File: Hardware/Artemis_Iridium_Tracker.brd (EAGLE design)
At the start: 50.8 x 63.5 mm, 197 parts, among them J1 IRIDIUM_9603N, J2 USB-C, J6 uFL, J7 ANTENNA-GROUNDEDEDGE_SMA, Q1 DMG3414U-7, Q2 DMG3415U-7, Q3 DMG3415U-7, Q4 2N2222, U1 CH340E_MSOP10, U10 MCP111T-240E/TT, U11 3.3V, U2 LTC3225EDDB#TRMPBF, U3 ADM4210-1, U4 UBLOX_ZOE_M8-0-10, U5 AS179-92LF, U6 MS8607-02BA01, U7 ARTEMIS_MODULESMD, U9 MCP73831, X1 32.768kHz, X2 32.768kHz

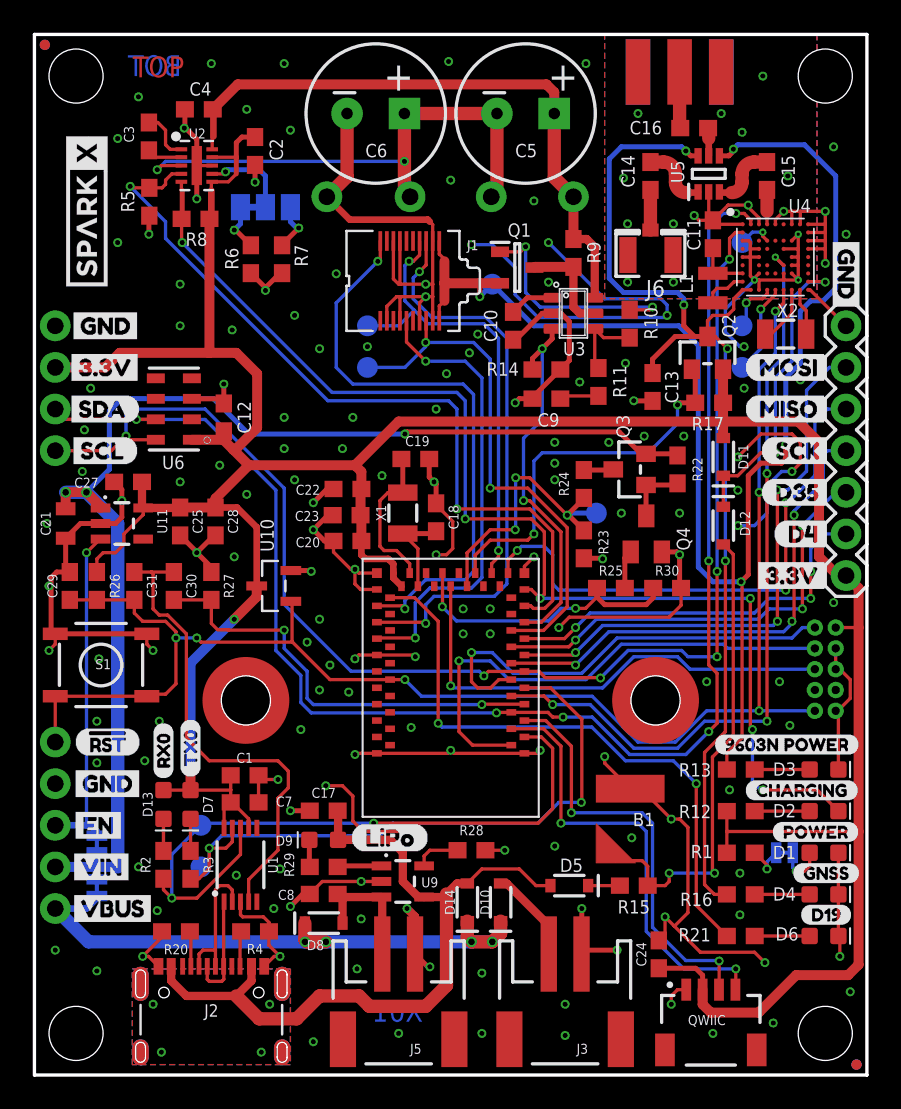
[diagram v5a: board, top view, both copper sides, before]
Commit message: Updated the PCB - tidied up the libraries
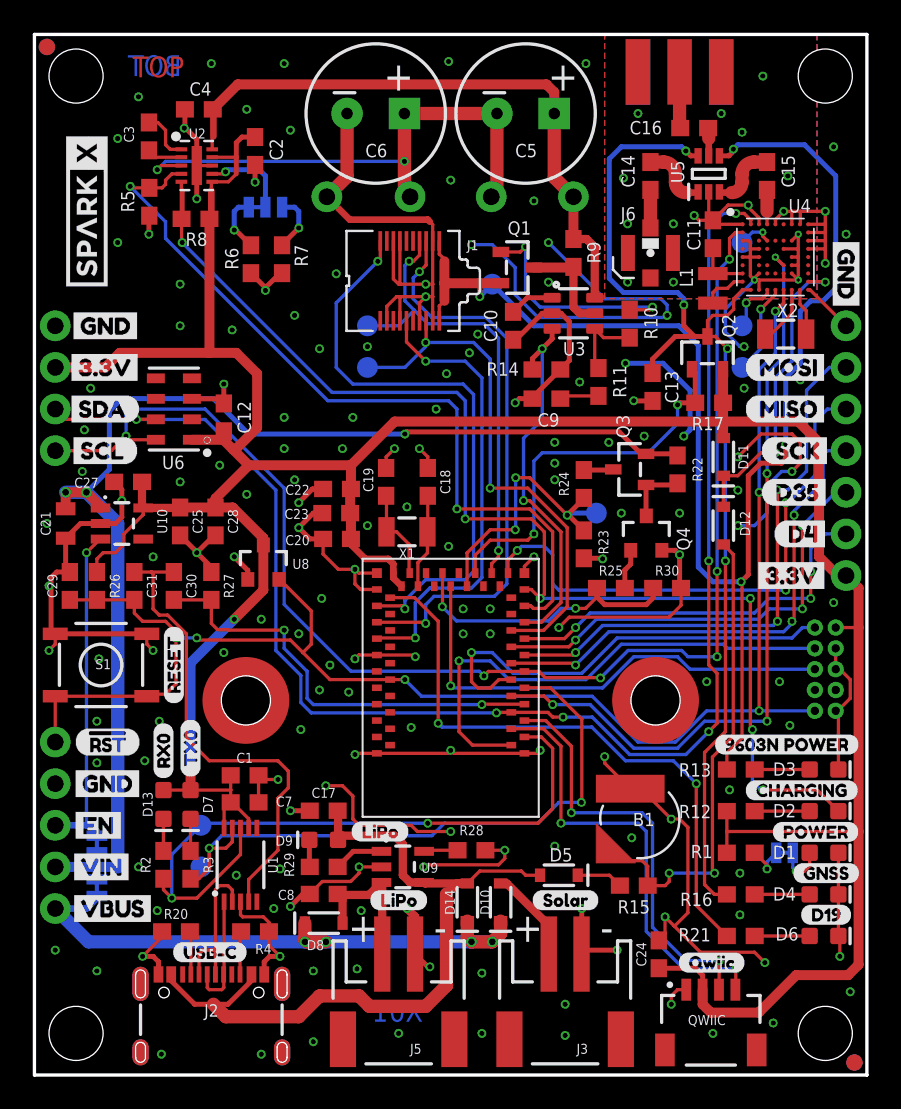
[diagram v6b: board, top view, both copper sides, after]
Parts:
- removed U11: 3.3V, SparkFun-IC-Power:SOT23-5
- added SPARKX1, SPARKX2: SPARKX-LOGO4, SparkX:SPARKX-MEDIUM
- added U$45, U$46: (no value), LiPo_0.03:LIPO0
- added U$53: (no value), USB-C:USB#C0
- added U$56: (no value), USB-C_0.03:USB#C0
- added U8: V_SUPERVISORBD48K24G-TL, New_Parts:SSOP3
- 3V3EN, MEAS: value (none) -> JUMPER-SMT_2_NC_TRACE_SILK
- I2C: device SparkX:1X04_NO_SILK -> SparkFun-Connectors:1X04_NO_SILK
- J1: device Qwiic_Iridium_9603N:IRIDIUM_9603N -> New_Parts:IRIDIUM_9603N
- J6: value uFL -> U.FL; device microbuilder:U.FL -> SparkFun-Connectors:U.FL
- J7: device Qwiic_Iridium_9603N:SMA-EDGE -> SparkFun-RF:SMA-EDGE
- JP1: value JUMPER-PAD-3-2OF3_NC_BY_TRACE_LARGE -> JUMPER-SMT_3_1-NC_TRACE_SILK; device Qwiic_Iridium_9603N:PAD-JUMPER-3-2OF3_NC_BY_TRACE_YES_SILK_LARGE -> SparkFun-Jumpers:SMT-JUMPER_3_1-NC_TRACE_SILK
- JP10, JP11, JP12, JP9: device SparkFun:STAND-OFF -> SparkFun-Hardware:STAND-OFF
- JP13, JP14, JP7, JP8: value FIDUCIALUFIDUCIAL -> FIDUCIAL1X2; device SparkFun:MICRO-FIDUCIAL -> SparkFun-Aesthetics:FIDUCIAL-1X2
- Q1: device DMG3414U-7:SOT96P240X100-3N -> New_Parts:SOT23-R
- Q2, Q3: device microbuilder:SOT23-WIDE -> New_Parts:SOT23-R
- Q4: value 2N2222 -> 600mA/40V; device transistor:SOT23-BEC -> SparkFun-DiscreteSemi:SOT23-3
- QWIIC: value (none) -> QWIIC_RIGHT_ANGLE
- R13, R5: device SparkFun-Resistors:0603@1 -> SparkFun-Resistors:0603
- R26, R27: device SparkFun-Resistors:0603@2 -> SparkFun-Resistors:0603
- R9: value 0.012 Ohm -> 0.012R; device SparkFun-Resistors:0603 -> New_Parts:0603
- SPI: device SparkFun-Connectors:1X07 -> SparkFun-Connectors:1X07_NO_SILK
- U$29: value SPARKX-LOGO4 -> (none); device SparkX:SPARKX-MEDIUM -> Solar_0.03:SOLAR0
- U$30: value SPARKX-LOGO4 -> (none); device SparkX:SPARKX-MEDIUM -> Qwiic_0.03:QWIIC0
- U$33: device RX:RX0 -> Rx:RX0
- U$37: device TX:TX0 -> Tx:TX0
- U$49: device LiPo:LIPO0 -> RESET_0.03:RESET0
- U10: value MCP111T-240E/TT -> 3.3V; device Microchip-MCP11:SOT95P237X112-3N -> SparkFun-IC-Power:SOT23-5
- U2: device Qwiic_Iridium_9603N:DFN300X200-10L -> New_Parts:DFN300X200-10L
- U3: device ADM4210:TSOT6 -> New_Parts:TSOT6
- U5: device SamacSys_Parts:SOT65P220X100-6N -> New_Parts:SOT65P220X100-6N
- U6: device SamacSys_Parts:MS8607-02BA01 -> New_Parts:MS8607-02BA01
- moved U$30 58.3 mm to (39.2, 6.86), turned to 0 degrees
- moved U$49 13.5 mm to (8.51, 22.6), turned to 90 degrees
- moved U10 10.0 mm to (5.33, 33.7), turned to 270 degrees
- moved U$29 8.56 mm to (30.4, 10.7), flipped to the top
- moved C19 2.26 mm to (21.5, 36.2), turned to 270 degrees
- moved C18 2.22 mm to (24.0, 36.2)
- moved X1 1.17 mm to (22.7, 33.1), turned to 0 degrees
- moved D5 0.90 mm to (32.0, 12.2)
- moved U9 0.89 mm to (22.5, 12.7)
- moved C23 0.65 mm to (18.4, 34.3)
- moved C20 0.65 mm to (18.5, 32.7)
- moved C22 0.63 mm to (18.5, 35.8)
- moved L1 0.38 mm to (41.4, 48.0)
- moved JP13 0.18 mm to (50.0, 0.76)
- moved JP14 0.18 mm to (0.76, 62.7)
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- renumbered RX(OUT) to RX1, TX(IN) to TX1
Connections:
- removed net SHLD: J2.SHLD1, J2.SHLD2, J2.SHLD3, J2.SHLD4, J2.SHLD5, J2.SHLD6, J2.SHLD7, J2.SHLD8
- net 3.3V: now also U10.5, U8.3; no longer U10.3, U11.5
- net ARTEMIS_!RESET: now also U8.2; no longer U10.1
- net GND: now also Q4.2, U8.1; no longer Q4.E, U11.2
- net IRIDIUM: now also J6.FEED; no longer J6.3
- net N$36: now also U10.3; no longer U11.3
- net N$37: now also Q4.3; no longer Q4.C
- net N$47: now also Q4.1; no longer Q4.B
- net VIN: now also U10.1; no longer U11.1
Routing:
- net GND: track 293.3 -> 307.7 mm, vias 169 -> 177
- net N$31: track 9.31 -> 5.67 mm
- net ARTEMIS_!RESET: track 92.6 -> 95.6 mm
- net V_BATT: track 8.15 -> 9.31 mm
- net D-2: track 8.48 -> 9.46 mm
- net N$20: track 1.94 -> 2.84 mm
- net N$39: track 2.79 -> 2.07 mm
- net V_USB: track 46.2 -> 46.8 mm
- net N$4: track 3.03 -> 3.61 mm
- net N$2: track 2.96 -> 3.54 mm
- net D+2: track 6.66 -> 7.18 mm
- removed copper zone on layer 1, net SHLD
- removed copper zone on layer 16, net SHLD

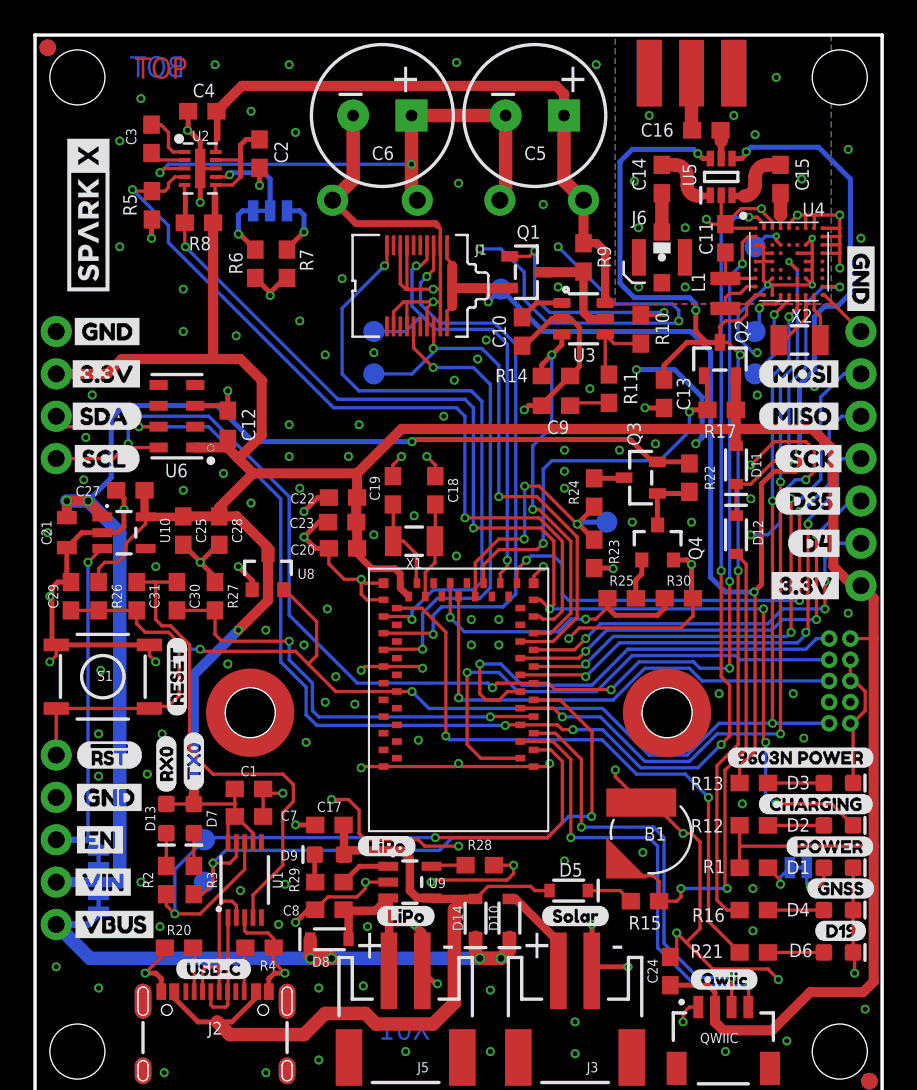
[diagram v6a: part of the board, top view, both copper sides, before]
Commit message: Updated the PCB and the examples README
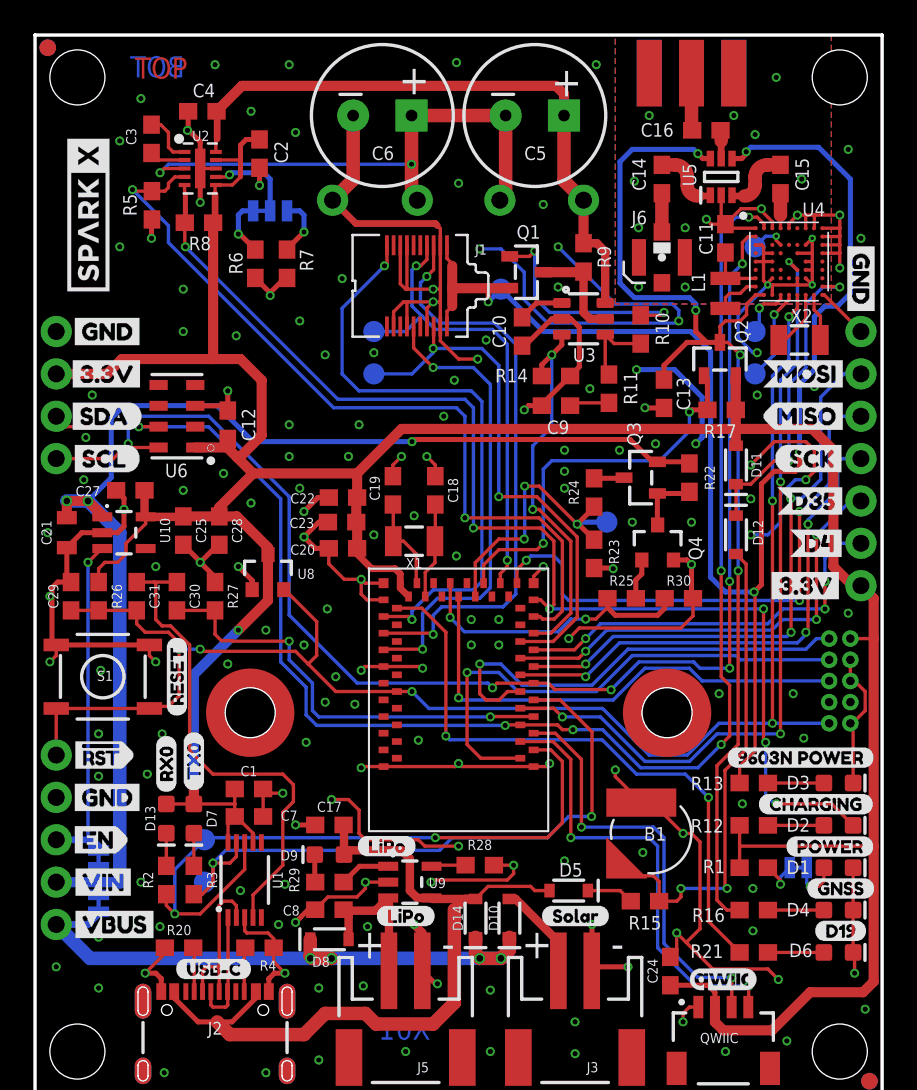
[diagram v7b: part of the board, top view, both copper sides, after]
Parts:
- removed U$28: (no value), MISO_BOT:MISO0
- removed U$30: (no value), Qwiic_0.03:QWIIC0
- removed U$51: (no value), D4:D40
- removed U$52: (no value), D4_BOT:D40
- removed U$54: (no value), D35:D350
- removed U$55: (no value), D35_BOT:D350
- removed U$66: (no value), Qwiic:QWIIC0
- removed U$8: (no value), MOSI:MOSI0
- added U$67: (no value), D35:D350
- added U$68: (no value), D35_m:D350
- added U$69: (no value), MISO:MISO0
- added U$70: (no value), MISO_m:MISO0
- added U$71: (no value), MOSI:MOSI0
- added U$72: (no value), MOSI_m:MOSI0
- added U$73: (no value), D4:D40
- added U$74: (no value), D4_m:D40
- U$11: device MISO:MISO0 -> SparkFun-Aesthetics:QWIIC_4MM
- U$25: device MOSI_BOT:MOSI0 -> SparkFun-Aesthetics:QWIIC_5MM
- U$58: device EN:EN0 -> RST:#RST0
- U$7: device RST:#RST0 -> EN:EN0
- moved U$25 42.4 mm to (41.3, 1.40)
- moved U$11 33.8 mm to (41.3, 6.86)
- moved U$7 5.09 mm to (1.91, 15.2)
- moved U$58 5.09 mm to (1.78, 20.3)
- moved U$59 0.13 mm to (1.91, 17.8)
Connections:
- net N$31 renamed XTALI
- net N$7 renamed XTALO
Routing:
- net GND: track 307.7 -> 311.3 mm, vias 177 -> 178
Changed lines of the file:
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@@
 <dimension x1="0" y1="63.5" x2="0" y2="0" x3="-7.62" y3="31.75" textsize="1.778" layer="51" unit="inch" precision="1"/>
 <dimension x1="0" y1="63.5" x2="50.8" y2="63.5" x3="25.4" y3="74.93" textsize="1.778" layer="51" unit="inch" precision="1"/>
-<text x="32.258" y="60.96" size="1.778" layer="21" ratio="18" align="center">+</text>
-<text x="22.225" y="60.96" size="1.778" layer="21" ratio="18" align="center">+</text>
+<text x="31.877" y="60.706" size="1.778" layer="21" ratio="18" align="center">+</text>
+<text x="22.733" y="60.833" size="1.778" layer="21" ratio="18" align="center">+</text>
 <polygon width="0.3048" layer="22" spacing="127" pour="hatch">
 <vertex x="25.23045625" y="19.939"/>
@@
 <element name="U$5" library="SCL_BOT" package="SCL0" value="" x="6.35" y="38.1" smashed="yes" rot="MR0"/>
 <element name="U$6" library="SDA_BOT" package="SDA0" value="" x="6.477" y="40.64" smashed="yes" rot="MR0"/>
-<element name="U$8" library="MOSI" package="MOSI0" value="" x="43.307" y="43.18" smashed="yes"/>
-<element name="U$11" library="MISO" package="MISO0" value="" x="43.307" y="40.64" smashed="yes"/>
 <element name="U$18" library="SCK" package="SCK0" value="" x="44.323" y="38.1" smashed="yes"/>
-<element name="U$25" library="MOSI_BOT" package="MOSI0" value="" x="48.768" y="43.18" smashed="yes" rot="MR0"/>
-<element name="U$28" library="MISO_BOT" package="MISO0" value="" x="48.768" y="40.64" smashed="yes" rot="MR0"/>
 <element name="U$31" library="SCK_BOT" package="SCK0" value="" x="48.895" y="38.1" smashed="yes" rot="MR0"/>
 <element name="U$19" library="GNSS" package="GNSS0" value="" x="46.228" y="12.319" smashed="yes"/>
@@
 <element name="U$47" library="3.3V EN" package="3#3V_EN0" value="" x="4.572" y="15.494" smashed="yes" rot="MR90"/>
 <element name="U$50" library="D19" package="D190" value="" x="46.736" y="9.779" smashed="yes"/>
-<element name="U$51" library="D4" package="D40" value="" x="45.085" y="33.02" smashed="yes"/>
-<element name="U$52" library="D4_BOT" package="D40" value="" x="48.768" y="33.02" smashed="yes" rot="MR0"/>
-<element name="U$54" library="D35" package="D350" value="" x="44.323" y="35.56" smashed="yes"/>
-<element name="U$55" library="D35_BOT" package="D350" value="" x="48.768" y="35.56" smashed="yes" rot="MR0"/>
 <element name="U10" library="SparkFun-IC-Power" package="SOT23-5" value="3.3V" x="5.334" y="33.655" smashed="yes" rot="R270">
 <attribute name="NAME" x="7.493" y="34.544" size="0.6096" layer="25" font="vector" ratio="20" rot="R270"/>
@@
 <element name="JP9" library="SparkFun-Hardware" package="STAND-OFF" value="STAND-OFF" x="2.54" y="60.96" smashed="yes"/>
 <element name="U$57" library="LiPo" package="LIPO0" value="" x="24.511" y="1.397" smashed="yes" rot="MR0"/>
-<element name="U$58" library="EN" package="EN0" value="" x="2.032" y="15.24" smashed="yes"/>
-<element name="U$59" library="GND" package="GND0" value="" x="2.032" y="17.78" smashed="yes"/>
+<element name="U$59" library="GND" package="GND0" value="" x="1.905" y="17.78" smashed="yes"/>
 <element name="U$60" library="VIN" package="VIN0" value="" x="1.905" y="12.7" smashed="yes"/>
 <element name="U$61" library="3xAA" package="3_X_AA0" value="" x="35.56" y="5.207" smashed="yes" rot="MR0"/>
@@
 <element name="U$64" library="Solar" package="SOLAR0" value="" x="35.052" y="7.112" smashed="yes" rot="MR0"/>
 <element name="U$65" library="VINdiv3" package="VIN#30" value="" x="34.163" y="35.052" smashed="yes" rot="MR90"/>
-<element name="U$66" library="Qwiic" package="QWIIC0" value="" x="44.069" y="1.397" smashed="yes" rot="MR0"/>
 <element name="C24" library="SparkFun-Capacitors" package="0603" value="1.0uF" x="38.1" y="7.366" smashed="yes" rot="R90">
 <attribute name="NAME" x="37.338" y="7.366" size="0.6096" layer="25" font="vector" ratio="20" rot="R90" align="bottom-center"/>
 <attribute name="PROD_ID" value="CAP-00868" x="38.1" y="8.636" size="1.778" layer="27" rot="R90" display="off"/>
 </element>
-<element name="U$7" library="RST" package="#RST0" value="" x="2.286" y="20.32" smashed="yes"/>
 <element name="U$16" library="TX0" package="TX00" value="" x="9.525" y="18.161" smashed="yes" rot="R90"/>
 <element name="U$23" library="RX0" package="RX00" value="" x="7.874" y="18.034" smashed="yes" rot="R90"/>
@@
 <attribute name="VALUE" x="40.132" y="48.895" size="0.6096" layer="27" font="vector" ratio="20" rot="R90" align="top-left"/>
 </element>
-<element name="U$30" library="Qwiic_0.03" package="QWIIC0" value="" x="39.243" y="6.858" smashed="yes"/>
 <element name="U$29" library="Solar_0.03" package="SOLAR0" value="" x="30.353" y="10.668" smashed="yes"/>
 <element name="U$45" library="LiPo_0.03" package="LIPO0" value="" x="20.447" y="10.668" smashed="yes"/>
@@
 <attribute name="VOLTAGE" value="2.4V" x="13.97" y="31.242" size="1.778" layer="27" display="off"/>
 </element>
+<element name="U$7" library="EN" package="EN0" value="" x="1.905" y="15.24" smashed="yes"/>
+<element name="U$58" library="RST" package="#RST0" value="" x="1.778" y="20.32" smashed="yes"/>
+<element name="U$67" library="D35" package="D350" value="" x="48.895" y="35.56" smashed="yes" rot="MR0"/>
+<element name="U$68" library="D35_m" package="D350" value="" x="44.45" y="35.56" smashed="yes"/>
+<element name="U$69" library="MISO" package="MISO0" value="" x="48.895" y="40.64" smashed="yes" rot="MR0"/>
+<element name="U$70" library="MISO_m" package="MISO0" value="" x="43.561" y="40.64" smashed="yes"/>
+<element name="U$71" library="MOSI" package="MOSI0" value="" x="43.561" y="43.18" smashed="yes"/>
+<element name="U$72" library="MOSI_m" package="MOSI0" value="" x="48.895" y="43.18" smashed="yes" rot="MR0"/>
+<element name="U$73" library="D4" package="D40" value="" x="45.212" y="33.02" smashed="yes"/>
+<element name="U$74" library="D4_m" package="D40" value="" x="48.895" y="33.02" smashed="yes" rot="MR0"/>
+<element name="U$11" library="SparkFun-Aesthetics" package="QWIIC_4MM" value="" x="41.275" y="6.858" smashed="yes"/>
+<element name="U$25" library="SparkFun-Aesthetics" package="QWIIC_5MM" value="" x="41.275" y="1.397" smashed="yes" rot="MR0"/>
 </elements>
 <signals>
@@
 <wire x1="13.02" y1="30.795" x2="12.192" y2="31.623" width="0.3048" layer="1"/>
 <via x="7.239" y="31.623" extent="1-16" drill="0.3"/>
+<wire x1="24.3032" y1="46.025" x2="24.3032" y2="45.1658" width="0.2032" layer="1"/>
+<wire x1="25.4" y1="44.069" x2="26.543" y2="44.069" width="0.2032" layer="1"/>
+<wire x1="24.3032" y1="45.1658" x2="25.4" y2="44.069" width="0.2032" layer="1"/>
+<via x="3.81" y="9.398" extent="1-16" drill="0.3"/>
 </signal>
 <signal name="EXT_PWR">
@@
 <wire x1="11.176" y1="27.178" x2="10.795" y2="27.559" width="0.2032" layer="1"/>
 </signal>
-<signal name="N$7">
+<signal name="XTALO">
 <contactref element="X1" pad="P$2"/>
 <contactref element="C18" pad="2"/>
@@
 <wire x1="24.003" y1="33.04" x2="23.983" y2="33.02" width="0.2032" layer="1"/>
 </signal>
-<signal name="N$31">
+<signal name="XTALI">
 <contactref element="X1" pad="P$1"/>
 <contactref element="C19" pad="2"/>
